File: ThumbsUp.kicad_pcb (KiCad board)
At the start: 2 copper layers, 250.9 x 280.9 mm, 172 parts, among them IC1 RP2040, IC2 W25Q128JVSIM, IC3 RP2040, IC4 W25Q128JVSIM, J1 Conn_01x04_Male, J10 Raiser_Male, J11 Raiser_Female, J12 Raiser_Male, J13 Raiser_Female, J14 Raiser_Male, J15 Raiser_Female, J16 Raiser_Male, J17 Raiser_Female, J18 Raiser_Male, J19 Raiser_Female, J2 Conn_01x04_Male, J20 Conn_01x04_Female, J21 Conn_01x04_Female, J22 Conn_01x04_Female, J23 Conn_01x04_Female, J24 Conn_01x04_Male, J25 Conn_01x04_Male, J26 Conn_01x04_Male, J27 Conn_01x04_Male, J28 Conn_01x04_Female, J29 Conn_01x04_Female, J3 Conn_01x04_Female, J30 Conn_01x04_Female, J31 Conn_01x04_Female, J32 USB_C_Receptacle_USB2.0, J33 Raiser_Male, J34 Raiser_Female, J35 Raiser_Male, J36 STX-3501-3N, J37 USB_C_Receptacle_USB2.0, J38 Raiser_Female, J39 Raiser_Male, J4 Conn_01x04_Male, J40 Raiser_Female, J41 Raiser_Male, J42 Raiser_Female, J43 Raiser_Male, J44 Raiser_Female, J45 Raiser_Male, J46 STX-3501-3N, J47 Raiser_Female, J48 Raiser_Male, J49 Raiser_Female, J5 Conn_01x04_Female, J50 Raiser_Male, J51 Raiser_Female, J52 Raiser_Male, J6 Conn_01x04_Male, J7 Conn_01x04_Male, J8 Conn_01x04_Male, J9 Raiser_Female, U1 NCP1117-3.3_SOT223, U2 NCP1117-3.3_SOT223, Y1 ABLS-12.000MHZ-B4-T, Y2 ABLS-12.000MHZ-B4-T

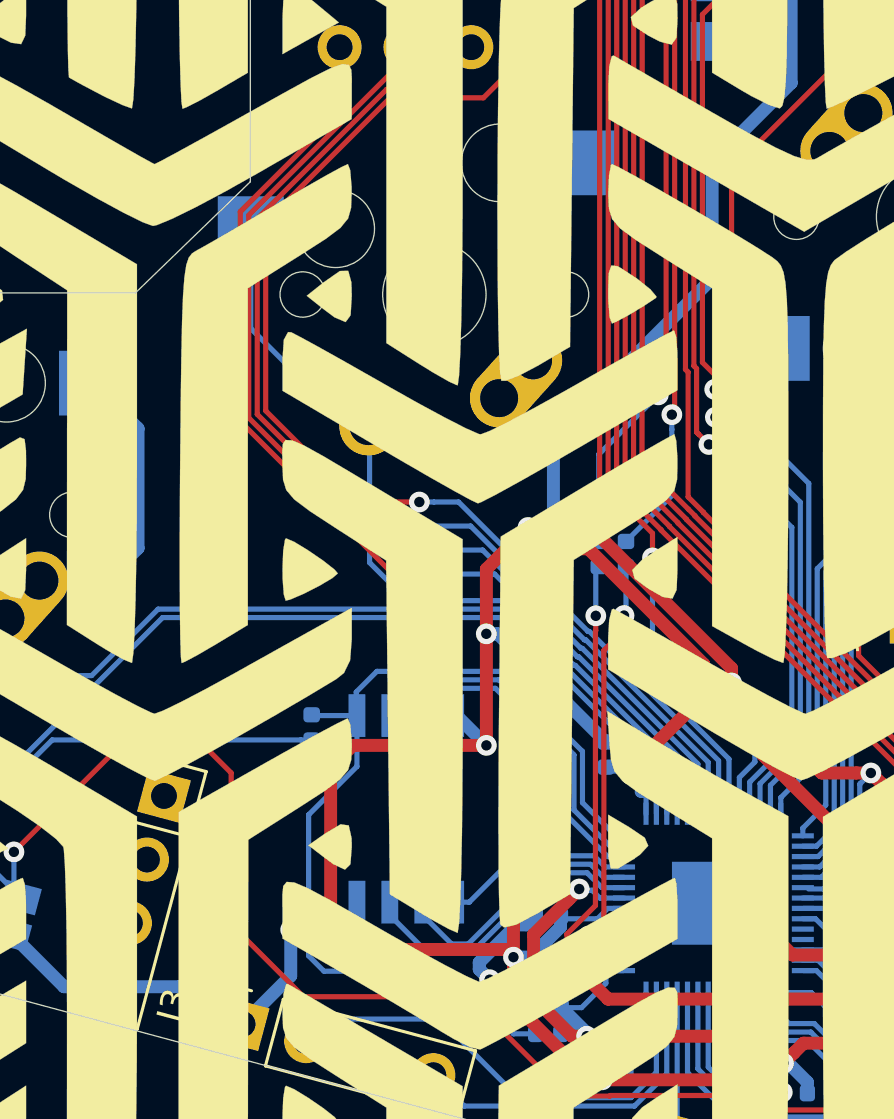
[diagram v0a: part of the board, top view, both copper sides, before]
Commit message: Minor tracks movements
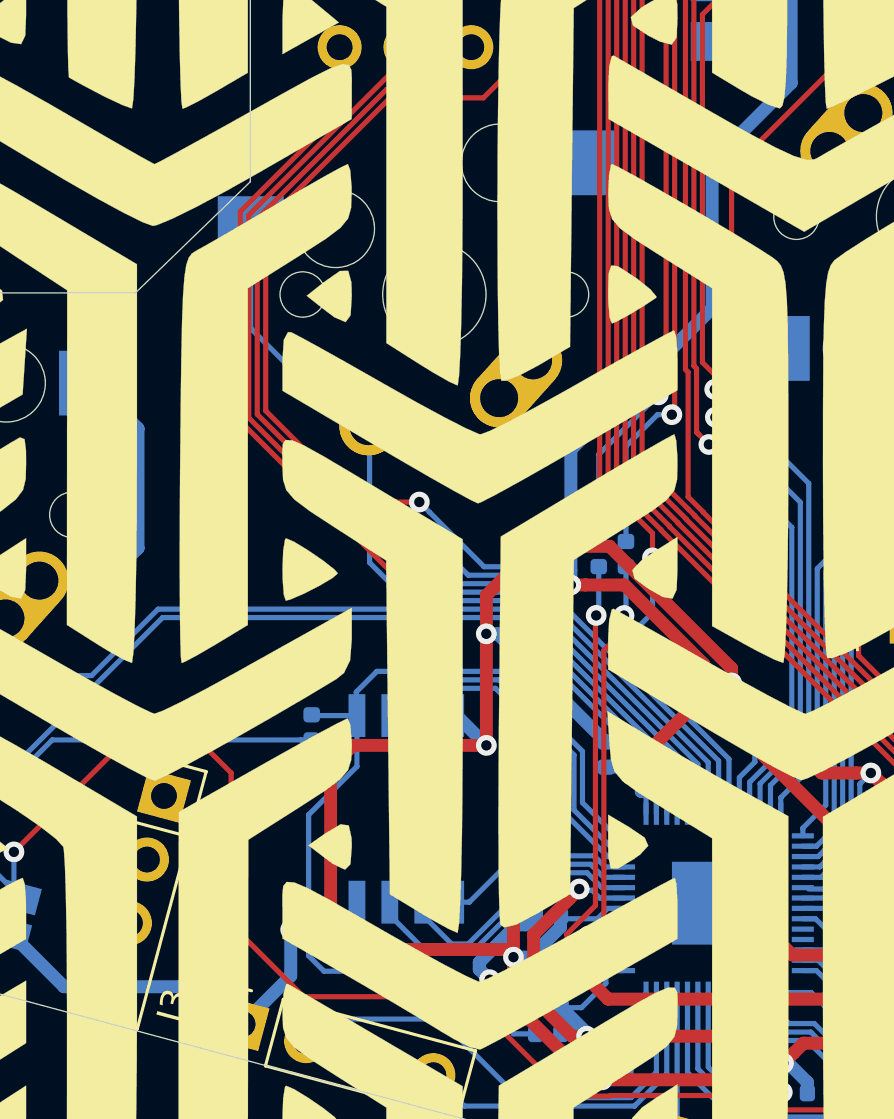
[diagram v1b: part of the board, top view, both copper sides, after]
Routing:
- net +3V3: track 254.6 -> 253.2 mm
- net L-BASE: track 423.5 -> 422.3 mm
- net K_F: track 56.2 -> 56.9 mm

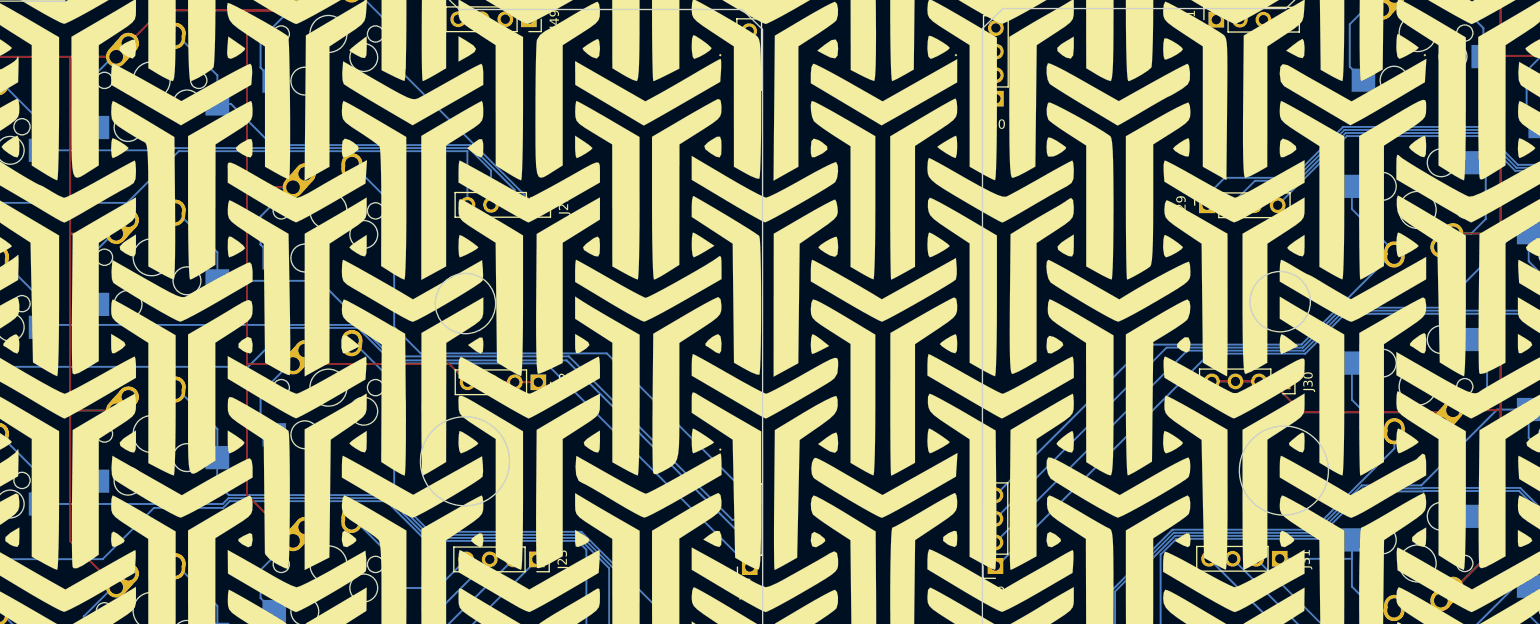
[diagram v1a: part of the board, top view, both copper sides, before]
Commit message: Added a raiser near USB connectors
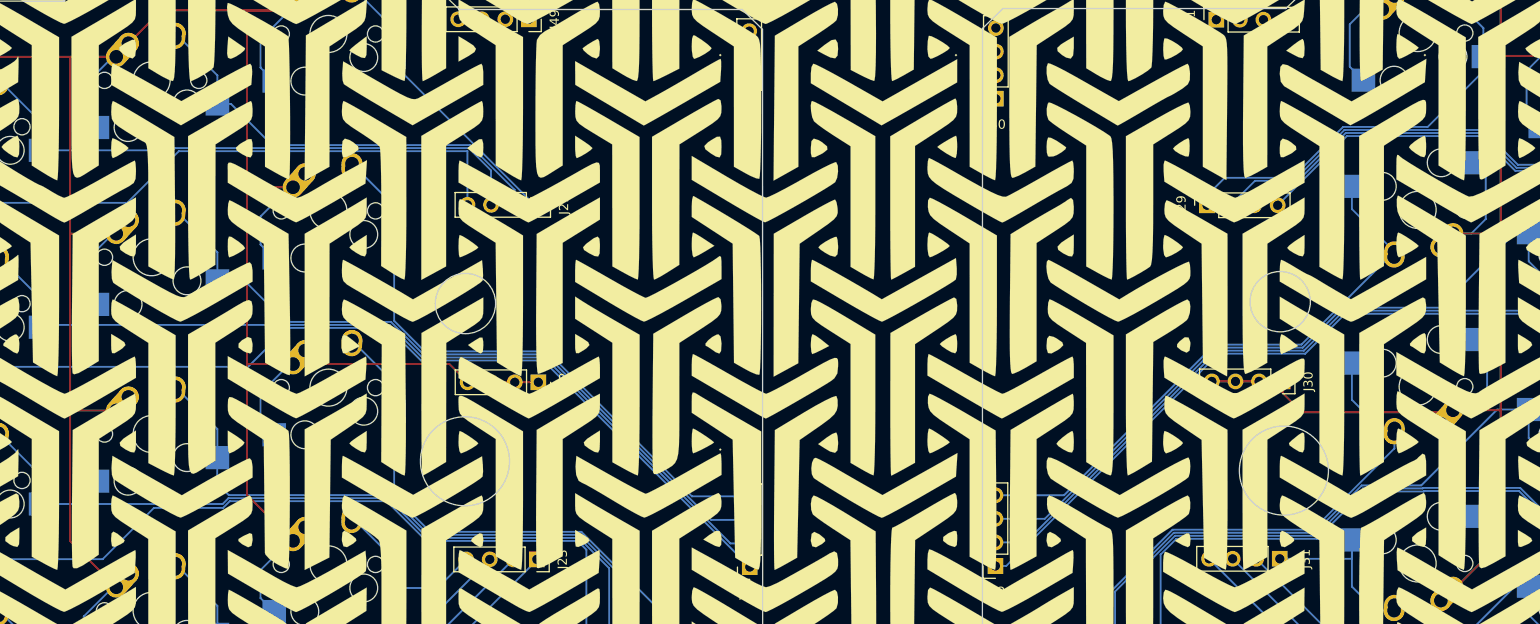
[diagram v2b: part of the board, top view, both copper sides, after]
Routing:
- net Net-(J29-Pad1): track 51.0 -> 47.5 mm

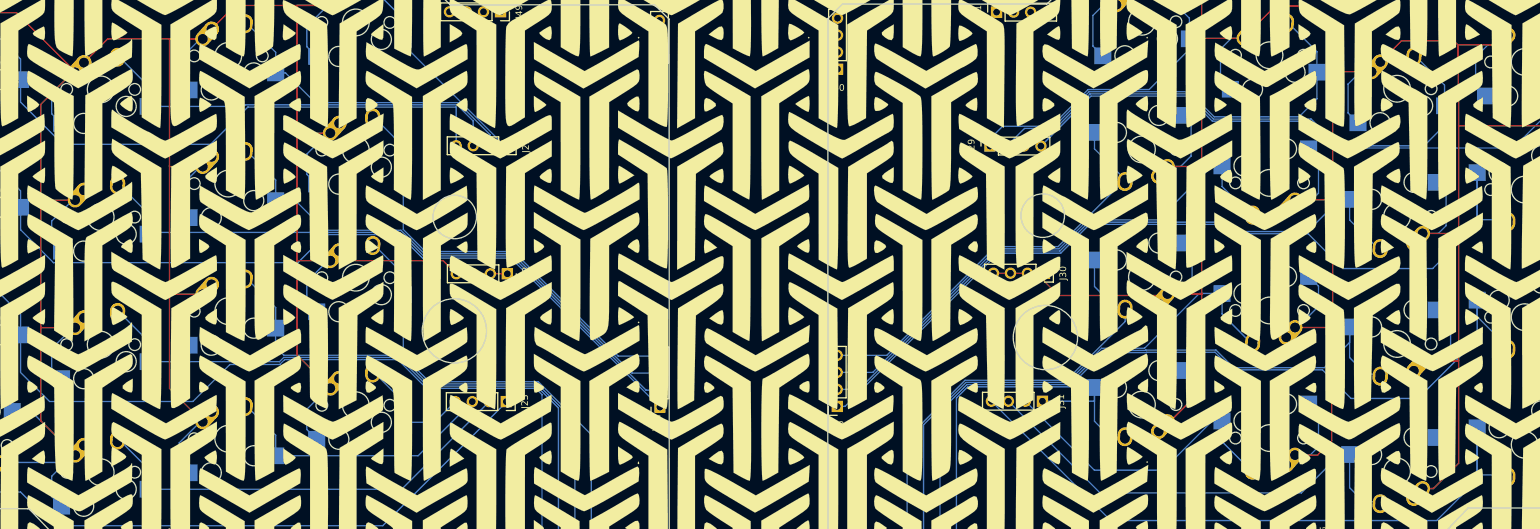
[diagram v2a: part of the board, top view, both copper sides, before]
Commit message: Minor tracks movements
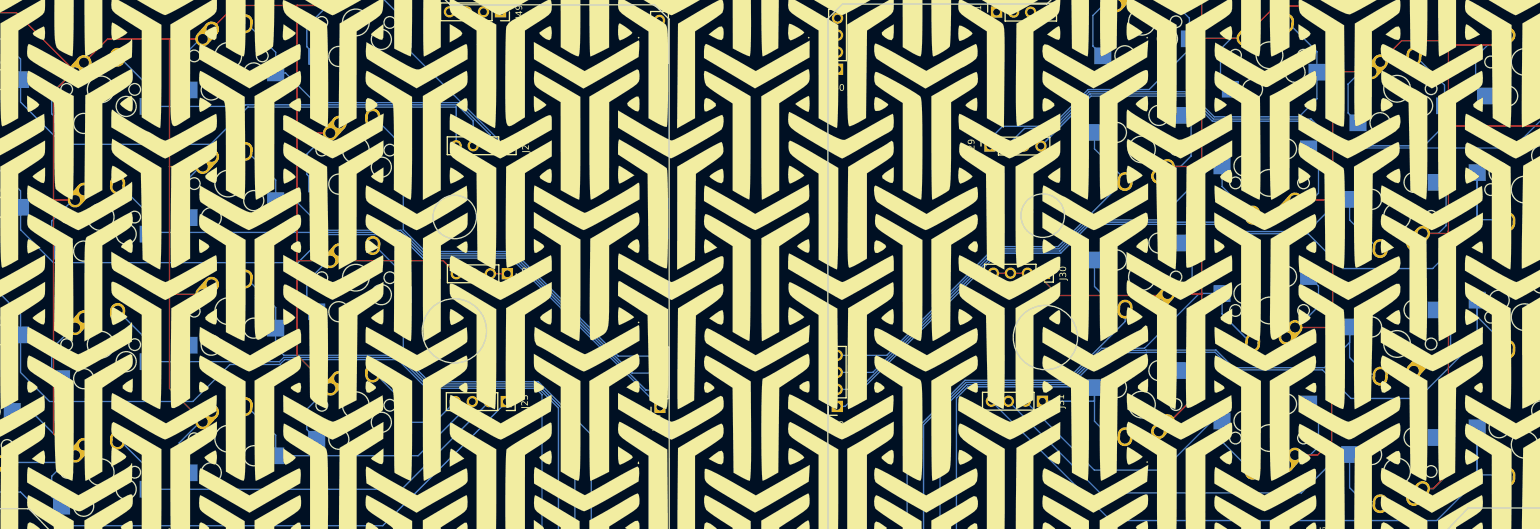
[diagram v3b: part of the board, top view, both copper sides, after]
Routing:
- net Net-(J22-Pad1): track 534.3 -> 528.9 mm
- net Net-(J30-Pad1): track 576.4 -> 573.1 mm
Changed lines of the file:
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@@
     (thickness 1.6)
     (drawings 141)
-    (tracks 2270)
+    (tracks 2269)
     (zones 0)
     (modules 172)
@@
   (segment (start 221.632987 545.450322) (end 224.779025 542.304284) (width 0.2) (layer B.Cu) (net 126))
   (segment (start 221.272025 545.450322) (end 221.632987 545.450322) (width 0.2) (layer B.Cu) (net 126))
-  (segment (start 245.7 509.367013) (end 245.65 509.317013) (width 0.2) (layer F.Cu) (net 126))
-  (segment (start 245.65 509.317013) (end 245.65 505) (width 0.2) (layer F.Cu) (net 126))
   (segment (start 226.96 507.26) (end 226.9 507.2) (width 0.2) (layer F.Cu) (net 126))
   (segment (start 232.702025 507.26) (end 226.96 507.26) (width 0.2) (layer F.Cu) (net 126))
   (segment (start 226.9 526.35) (end 226.9 507.2) (width 0.2) (layer F.Cu) (net 126))
   (segment (start 226.9 507.2) (end 226.9 501.45) (width 0.2) (layer F.Cu) (net 126))
-  (segment (start 245.599678 531.400322) (end 245.7 531.3) (width 0.2) (layer F.Cu) (net 126))
-  (segment (start 240.322025 531.400322) (end 245.599678 531.400322) (width 0.2) (layer F.Cu) (net 126))
-  (segment (start 245.599678 550.450322) (end 245.7 550.35) (width 0.2) (layer F.Cu) (net 126))
-  (segment (start 240.322026 550.450322) (end 245.599678 550.450322) (width 0.2) (layer F.Cu) (net 126))
-  (segment (start 245.7 550.35) (end 245.7 531.3) (width 0.2) (layer F.Cu) (net 126))
   (segment (start 242.430322 542.830322) (end 242.354026 542.830322) (width 0.2) (layer B.Cu) (net 126))
   (segment (start 244.5 544.9) (end 242.430322 542.830322) (width 0.2) (layer B.Cu) (net 126))
@@
   (segment (start 240.322026 550.450322) (end 243.149678 550.450322) (width 0.2) (layer B.Cu) (net 126))
   (segment (start 243.149678 550.450322) (end 244.5 549.1) (width 0.2) (layer B.Cu) (net 126))
-  (segment (start 245.7 531.3) (end 245.7 515.35) (width 0.2) (layer F.Cu) (net 126))
-  (segment (start 245.7 515.35) (end 245.7 509.367013) (width 0.2) (layer F.Cu) (net 126))
-  (segment (start 245.65 503.26) (end 245.65 505) (width 0.2) (layer F.Cu) (net 126))
-  (segment (start 251.752025 503.26) (end 245.65 503.26) (width 0.2) (layer F.Cu) (net 126))
-  (segment (start 237.162025 502.65) (end 234.012025 505.8) (width 0.2) (layer F.Cu) (net 126))
-  (segment (start 245 502.65) (end 237.162025 502.65) (width 0.2) (layer F.Cu) (net 126))
-  (segment (start 245.65 505) (end 245.65 503.3) (width 0.2) (layer F.Cu) (net 126))
-  (segment (start 245.65 503.3) (end 245 502.65) (width 0.2) (layer F.Cu) (net 126))
   (segment (start 249.5 515.35) (end 245.7 515.35) (width 0.2) (layer F.Cu) (net 126))
   (segment (start 261.85 515.35) (end 249.5 515.35) (width 0.2) (layer F.Cu) (net 126))
@@
   (segment (start 240.322025 569.500323) (end 241.924677 569.500323) (width 0.2) (layer B.Cu) (net 126))
   (segment (start 241.924677 569.500323) (end 243.829025 567.595975) (width 0.2) (layer B.Cu) (net 126))
-  (segment (start 245.7 565.725) (end 245.7 550.35) (width 0.2) (layer F.Cu) (net 126))
-  (segment (start 240.322025 569.500323) (end 241.924677 569.500323) (width 0.2) (layer F.Cu) (net 126))
-  (segment (start 241.924677 569.500323) (end 245.7 565.725) (width 0.2) (layer F.Cu) (net 126))
   (segment (start 242.379025 523.780322) (end 242.354025 523.780322) (width 0.2) (layer B.Cu) (net 126))
   (segment (start 243.829025 525.230322) (end 242.379025 523.780322) (width 0.2) (layer B.Cu) (net 126))
@@
   (segment (start 221.272025 526.400323) (end 223.774677 526.400323) (width 0.2) (layer B.Cu) (net 126))
   (segment (start 223.774677 526.400323) (end 224.779025 525.395975) (width 0.2) (layer B.Cu) (net 126))
+  (segment (start 245.7 515.35) (end 244.17 515.35) (width 0.2) (layer F.Cu) (net 126))
+  (segment (start 237.162025 502.65) (end 234.012025 505.8) (width 0.2) (layer F.Cu) (net 126))
+  (segment (start 244.17 502.722) (end 244.098 502.65) (width 0.2) (layer F.Cu) (net 126))
+  (segment (start 244.17 515.35) (end 244.17 502.722) (width 0.2) (layer F.Cu) (net 126))
+  (segment (start 244.098 502.65) (end 237.162025 502.65) (width 0.2) (layer F.Cu) (net 126))
+  (segment (start 244.25 503.26) (end 244.17 503.34) (width 0.2) (layer F.Cu) (net 126))
+  (segment (start 251.752025 503.26) (end 244.25 503.26) (width 0.2) (layer F.Cu) (net 126))
+  (segment (start 244.17 531.28) (end 244.17 515.35) (width 0.2) (layer F.Cu) (net 126))
+  (segment (start 244.049678 531.400322) (end 244.17 531.28) (width 0.2) (layer F.Cu) (net 126))
+  (segment (start 240.322025 531.400322) (end 244.049678 531.400322) (width 0.2) (layer F.Cu) (net 126))
+  (segment (start 244.049678 550.450322) (end 244.17 550.33) (width 0.2) (layer F.Cu) (net 126))
+  (segment (start 240.322026 550.450322) (end 244.049678 550.450322) (width 0.2) (layer F.Cu) (net 126))
+  (segment (start 241.924677 569.500323) (end 240.322025 569.500323) (width 0.2) (layer F.Cu) (net 126))
+  (segment (start 244.17 531.026) (end 244.17 567.255) (width 0.2) (layer F.Cu) (net 126))
+  (segment (start 244.17 567.255) (end 241.924677 569.500323) (width 0.2) (layer F.Cu) (net 126))
   (segment (start 193.915322 562.040322) (end 195.872025 562.040322) (width 0.2) (layer B.Cu) (net 127))
   (segment (start 191.327025 554.420322) (end 191.327025 559.452025) (width 0.2) (layer B.Cu) (net 127))
@@
   (segment (start 53.2 502.36) (end 53.2 521.35) (width 0.2) (layer F.Cu) (net 187))
   (segment (start 58.172789 502.36) (end 53.2 502.36) (width 0.2) (layer F.Cu) (net 187))
-  (segment (start 34 559.400163) (end 39.122789 564.522952) (width 0.2) (layer F.Cu) (net 187))
-  (segment (start 39.122789 507.36) (end 38.761827 507.36) (width 0.2) (layer F.Cu) (net 187))
-  (segment (start 38.761827 507.36) (end 34 512.121827) (width 0.2) (layer F.Cu) (net 187))
-  (segment (start 34.122952 545.472952) (end 34 545.35) (width 0.2) (layer F.Cu) (net 187))
-  (segment (start 39.12279 545.472952) (end 34.122952 545.472952) (width 0.2) (layer F.Cu) (net 187))
-  (segment (start 34 545.35) (end 34 559.400163) (width 0.2) (layer F.Cu) (net 187))
-  (segment (start 34.022952 526.422952) (end 34 526.4) (width 0.2) (layer F.Cu) (net 187))
-  (segment (start 39.122789 526.422952) (end 34.022952 526.422952) (width 0.2) (layer F.Cu) (net 187))
-  (segment (start 34 512.121827) (end 34 526.4) (width 0.2) (layer F.Cu) (net 187))
-  (segment (start 34 526.4) (end 34 545.35) (width 0.2) (layer F.Cu) (net 187))
   (segment (start 39.122789 507.21) (end 30.362789 498.45) (width 0.2) (layer F.Cu) (net 187))
   (segment (start 39.122789 507.36) (end 39.122789 507.21) (width 0.2) (layer F.Cu) (net 187))
@@
   (segment (start 39.122789 564.522952) (end 38.727048 564.522952) (width 0.2) (layer B.Cu) (net 187))
   (segment (start 38.727048 564.522952) (end 37.647048 565.602952) (width 0.2) (layer B.Cu) (net 187))
+  (segment (start 35.89 526.391904) (end 35.881904 526.4) (width 0.2) (layer F.Cu) (net 187))
+  (segment (start 35.89 510.231827) (end 35.89 526.391904) (width 0.2) (layer F.Cu) (net 187))
+  (segment (start 39.122789 507.36) (end 38.761827 507.36) (width 0.2) (layer F.Cu) (net 187))
+  (segment (start 38.761827 507.36) (end 35.89 510.231827) (width 0.2) (layer F.Cu) (net 187))
+  (segment (start 35.921048 526.422952) (end 35.89 526.454) (width 0.2) (layer F.Cu) (net 187))
+  (segment (start 39.122789 526.422952) (end 35.921048 526.422952) (width 0.2) (layer F.Cu) (net 187))
+  (segment (start 35.89 526.4) (end 35.89 526.454) (width 0.2) (layer F.Cu) (net 187))
+  (segment (start 35.89 526.454) (end 35.89 545.35) (width 0.2) (layer F.Cu) (net 187))
+  (segment (start 35.89 561.290163) (end 39.122789 564.522952) (width 0.2) (layer F.Cu) (net 187))
+  (segment (start 35.89 545.35) (end 35.89 561.290163) (width 0.2) (layer F.Cu) (net 187))
+  (segment (start 38.999838 545.35) (end 39.12279 545.472952) (width 0.2) (layer F.Cu) (net 187))
+  (segment (start 35.89 545.35) (end 38.999838 545.35) (width 0.2) (layer F.Cu) (net 187))
   (segment (start 36 575.05) (end 30.967789 570.017789) (width 0.2) (layer B.Cu) (net 188))
   (segment (start 85.05 575.05) (end 36 575.05) (width 0.2) (layer B.Cu) (net 188))

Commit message: Added cuts to break-out the outer columns
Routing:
- net Net-(J30-Pad1): track 573.1 -> 589.8 mm
- net Net-(J44-Pad1): track 122.2 -> 135.0 mm
- net Net-(J22-Pad1): track 528.9 -> 536.0 mm
- net Net-(J11-Pad4): track 144.4 -> 150.7 mm
- net Net-(J21-Pad4): track 88.6 -> 93.1 mm
- net Net-(J15-Pad1): track 142.7 -> 144.8 mm
- net Net-(J29-Pad3): track 82.9 -> 81.8 mm
- net Net-(J29-Pad4): track 100.1 -> 99.0 mm
- net Net-(J31-Pad4): track 101.9 -> 102.6 mm
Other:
- outline, holes or cut-outs redrawn
